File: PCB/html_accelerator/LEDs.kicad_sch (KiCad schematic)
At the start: 4 parts

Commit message: 3d part models, PCB netlist imported
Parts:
- C28, C33: footprint (none) -> Capacitor_SMD:C_0805_2012Metric_Pad1.18x1.45mm_HandSolder
- D2: footprint (none) -> LED_SMD:LED_0805_2012Metric_Pad1.15x1.40mm_HandSolder
- R20: footprint (none) -> Resistor_SMD:R_0805_2012Metric_Pad1.20x1.40mm_HandSolder
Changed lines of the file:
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@@
       (effects (font (size 1.27 1.27)) (justify left))
     )
-    (property "Footprint" "" (at 59.69 88.9 0)
+    (property "Footprint" "Capacitor_SMD:C_0805_2012Metric_Pad1.18x1.45mm_HandSolder" (at 59.69 88.9 0)
       (effects (font (size 1.27 1.27)) hide)
     )
@@
       (effects (font (size 1.27 1.27)))
     )
-    (property "Footprint" "" (at 72.644 84.074 90)
+    (property "Footprint" "Resistor_SMD:R_0805_2012Metric_Pad1.20x1.40mm_HandSolder" (at 72.644 84.074 90)
       (effects (font (size 1.27 1.27)) hide)
     )
@@
       (effects (font (size 1.27 1.27)) (justify left))
     )
-    (property "Footprint" "" (at 68.58 41.91 0)
+    (property "Footprint" "LED_SMD:LED_0805_2012Metric_Pad1.15x1.40mm_HandSolder" (at 68.58 41.91 0)
       (effects (font (size 1.27 1.27)) hide)
     )
@@
       (effects (font (size 1.27 1.27)) (justify left))
     )
-    (property "Footprint" "" (at 79.7052 87.63 0)
-      (effects (font (size 1.27 1.27)) hide)
-    )
+    (property "Footprint" "Capacitor_SMD:C_0805_2012Metric_Pad1.18x1.45mm_HandSolder" (at 79.7052 87.63 0)
+      (effects (font (size 1.27 1.27)) hide)
+    )

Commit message: placement updates
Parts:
- C33: footprint Capacitor_SMD:C_0805_2012Metric_Pad1.18x1.45mm_HandSolder -> Capacitor_SMD:CP_Elec_6.3x5.8
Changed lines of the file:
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@@
       (effects (font (size 1.27 1.27)) (justify left))
     )
-    (property "Footprint" "Capacitor_SMD:C_0805_2012Metric_Pad1.18x1.45mm_HandSolder" (at 59.69 88.9 0)
+    (property "Footprint" "Capacitor_SMD:CP_Elec_6.3x5.8" (at 59.69 88.9 0)
       (effects (font (size 1.27 1.27)) hide)
     )
@@
         (path "/12b3a7c9-141f-40ba-9ebb-094b58bfa6c7/d3bc6377-21cd-485e-9e5e-2f9ae5072344"
           (reference "C67") (unit 1)
+        )
+        (path "/12b3a7c9-141f-40ba-9ebb-094b58bfa6c7/7615f50f-5ee8-4f8e-abfe-c09f3fbb9ceb"
+          (reference "C24") (unit 1)
         )
       )
@@
       (effects (font (size 1.27 1.27)) hide)
     )
-    (property "Datasheet" "1%" (at 73.66 83.82 0)
+    (property "Datasheet" "~" (at 73.66 83.82 0)
       (effects (font (size 1.27 1.27)) hide)
     )
@@
           (reference "R66") (unit 1)
         )
+        (path "/12b3a7c9-141f-40ba-9ebb-094b58bfa6c7/7615f50f-5ee8-4f8e-abfe-c09f3fbb9ceb"
+          (reference "R58") (unit 1)
+        )
       )
     )
@@
           (reference "#PWR0117") (unit 1)
         )
+        (path "/12b3a7c9-141f-40ba-9ebb-094b58bfa6c7/7615f50f-5ee8-4f8e-abfe-c09f3fbb9ceb"
+          (reference "#PWR040") (unit 1)
+        )
       )
     )
@@
           (reference "#PWR0114") (unit 1)
         )
-      )
-    )
-  )
-  (symbol (lib_id "power:+3V3") (at 46.99 30.48 0) (unit 1)
-    (in_bom yes) (on_board yes) (dnp no)
-    (property "Reference" "#PWR03" (at 46.99 34.29 0)
-      (effects (font (size 1.27 1.27)) hide)
-    )
-    (property "Value" "+5v_USB" (at 46.99 25.7081 0)
-      (effects (font (size 1.27 1.27)))
-    )
-    (property "Footprint" "" (at 46.99 30.48 0)
-      (effects (font (size 1.27 1.27)) hide)
-    )
-    (property "Datasheet" "" (at 46.99 30.48 0)
-      (effects (font (size 1.27 1.27)) hide)
-    )
-    (pin "1")
-    (instances
-      (project "html_accelerator"
-        (path "/12b3a7c9-141f-40ba-9ebb-094b58bfa6c7/3421334e-11b3-46c8-b0f2-353f0fa6f362"
-          (reference "#PWR03") (unit 1)
-        )
-        (path "/12b3a7c9-141f-40ba-9ebb-094b58bfa6c7/8c9bd1fc-c6d3-45cd-babe-9d9e8ea6549d"
-          (reference "#PWR014") (unit 1)
-        )
-        (path "/12b3a7c9-141f-40ba-9ebb-094b58bfa6c7/665af54b-4239-4192-942b-b320317cb76f"
-          (reference "#PWR062") (unit 1)
-        )
-        (path "/12b3a7c9-141f-40ba-9ebb-094b58bfa6c7/c1e0624f-11bc-46dd-864f-01b3a932cae6"
-          (reference "#PWR066") (unit 1)
-        )
-        (path "/12b3a7c9-141f-40ba-9ebb-094b58bfa6c7/a3cdbafc-e5e5-4b5b-8c38-75acb12ca284"
-          (reference "#PWR081") (unit 1)
-        )
-        (path "/12b3a7c9-141f-40ba-9ebb-094b58bfa6c7/e4cf78dc-8e0c-4eaf-ac6f-547ec39b6f59"
-          (reference "#PWR092") (unit 1)
-        )
-        (path "/12b3a7c9-141f-40ba-9ebb-094b58bfa6c7/e85df621-c9d6-4c41-83df-274e70c69afa"
-          (reference "#PWR0103") (unit 1)
-        )
-        (path "/12b3a7c9-141f-40ba-9ebb-094b58bfa6c7/d3bc6377-21cd-485e-9e5e-2f9ae5072344"
-          (reference "#PWR0111") (unit 1)
+        (path "/12b3a7c9-141f-40ba-9ebb-094b58bfa6c7/7615f50f-5ee8-4f8e-abfe-c09f3fbb9ceb"
+          (reference "#PWR048") (unit 1)
         )
       )
@@
         (path "/12b3a7c9-141f-40ba-9ebb-094b58bfa6c7/d3bc6377-21cd-485e-9e5e-2f9ae5072344"
           (reference "D2") (unit 1)
+        )
+        (path "/12b3a7c9-141f-40ba-9ebb-094b58bfa6c7/7615f50f-5ee8-4f8e-abfe-c09f3fbb9ceb"
+          (reference "D3") (unit 1)
         )
       )
@@
           (reference "C66") (unit 1)
         )
-      )
+        (path "/12b3a7c9-141f-40ba-9ebb-094b58bfa6c7/7615f50f-5ee8-4f8e-abfe-c09f3fbb9ceb"
+          (reference "C23") (unit 1)
+        )
+      )
+    )
+  )
+  (symbol (lib_id "power:+5V") (at 46.99 30.48 0) (unit 1)
+    (in_bom yes) (on_board yes) (dnp no) (fields_autoplaced)
+    (property "Reference" "#PWR015" (at 46.99 34.29 0)
+      (effects (font (size 1.27 1.27)) hide)
+    )
+    (property "Value" "+5V" (at 46.99 26.9781 0)
+      (effects (font (size 1.27 1.27)))
+    )
+    (property "Footprint" "" (at 46.99 30.48 0)
+      (effects (font (size 1.27 1.27)) hide)
+    )
+    (property "Datasheet" "" (at 46.99 30.48 0)
+      (effects (font (size 1.27 1.27)) hide)
+    )
+    (pin "1")
+    (instances
+      (project "html_accelerator"
+        (path "/12b3a7c9-141f-40ba-9ebb-094b58bfa6c7/665af54b-4239-4192-942b-b320317cb76f"
+          (reference "#PWR015") (unit 1)
+        )
+        (path "/12b3a7c9-141f-40ba-9ebb-094b58bfa6c7/c1e0624f-11bc-46dd-864f-01b3a932cae6"
+          (reference "#PWR019") (unit 1)
+        )
+        (path "/12b3a7c9-141f-40ba-9ebb-094b58bfa6c7/d3bc6377-21cd-485e-9e5e-2f9ae5072344"
+          (reference "#PWR050") (unit 1)
+        )
+        (path "/12b3a7c9-141f-40ba-9ebb-094b58bfa6c7/7615f50f-5ee8-4f8e-abfe-c09f3fbb9ceb"
+          (reference "#PWR039") (unit 1)
+        )
+      )

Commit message: layout and 3d updates
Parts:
- removed C28: 0.1uF, Capacitor_SMD:C_0805_2012Metric_Pad1.18x1.45mm_HandSolder, symbol Device:C
- removed C33: 470uF, Capacitor_SMD:CP_Elec_6.3x5.8, symbol Device:C_Polarized_US
- removed R20: 3k, Resistor_SMD:R_0805_2012Metric_Pad1.20x1.40mm_HandSolder, symbol Device:R_US
- added D3, D4, D5: RED, LED_SMD:LED_0805_2012Metric_Pad1.15x1.40mm_HandSolder, symbol Device:LED
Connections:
- net +5V: now also D2.2 (A), D3.2 (A), D4.2 (A), D5.2 (A)
- net USB0_LED: now also D2.1 (K)
- net USB1_LED: now also D3.1 (K)
- net USB2_LED: now also D4.1 (K)
- net USB3_LED: now also D5.1 (K)
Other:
- moved on the sheet: D2

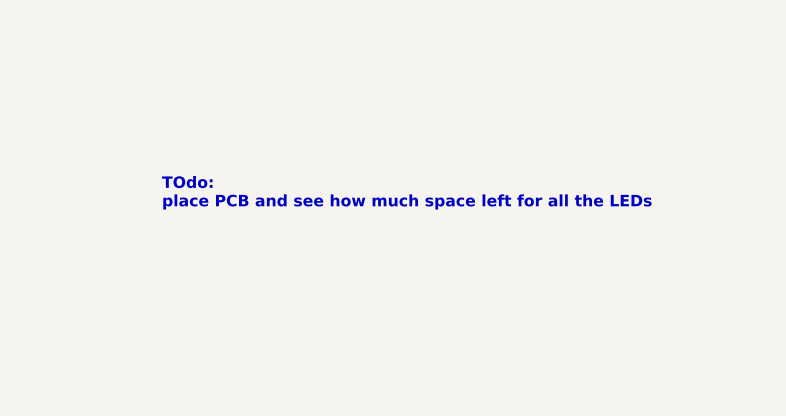
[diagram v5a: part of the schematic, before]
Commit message: Additional routing greebles, cleanup and gerber export with BOM
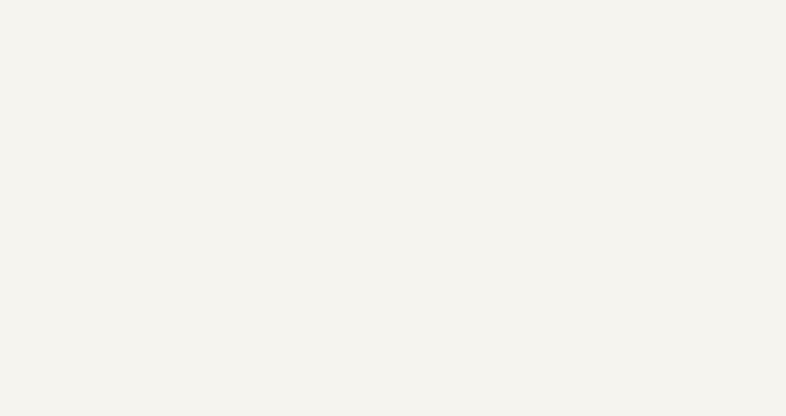
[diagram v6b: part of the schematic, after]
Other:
- note removed: "TOdo: place PCB and see how much space left for all the LEDs"
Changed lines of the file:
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@@
 		(rev "1")
-	)
-	(text "TOdo:\nplace PCB and see how much space left for all the LEDs"
-		(exclude_from_sim no)
-		(at 115.57 62.23 0)
-		(effects
-			(font
-				(size 1.27 1.27)
-				(bold yes)
-			)
-			(justify left bottom)
-		)
 	)
 	(junction
@@
 			)
 		)
-		(property "Description" ""
+		(property "Description" "Light emitting diode"
 			(at 55.88 77.47 0)
+			(hide yes)
 			(show_name no)
 			(do_not_autoplace no)
@@
 			)
 		)
-		(property "Description" ""
+		(property "Description" "Light emitting diode"
 			(at 55.88 68.58 0)
+			(hide yes)
 			(show_name no)
 			(do_not_autoplace no)
@@
 			)
 		)
-		(property "Description" ""
+		(property "Description" "Light emitting diode"
 			(at 55.88 59.69 0)
+			(hide yes)
 			(show_name no)
 			(do_not_autoplace no)
@@
 			)
 		)
-		(property "Description" ""
+		(property "Description" "Light emitting diode"
 			(at 55.88 50.8 0)
-			(show_name no)
-			(do_not_autoplace no)
+			(hide yes)
+			(show_name no)
+			(do_not_autoplace no)

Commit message: gerbers and readme updates
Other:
- company: (none) -> Spencer K
- title: USB, 5v POWER -> HTML Accelerator
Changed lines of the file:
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@@
 	(paper "A4")
 	(title_block
-		(title "USB, 5v POWER")
-		(date "2024-09-15")
-		(rev "1")
+		(title "HTML Accelerator")
+		(date "2026-04-25")
+		(rev "1.0")
+		(company "Spencer K")
+		(comment 1 "https://github.com/akaStanley/HTML_Accelerator")
 	)
 	(junction
